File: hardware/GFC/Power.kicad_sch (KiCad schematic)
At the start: 22 parts, among them J1 BAT, U1 MAX17048G+T10

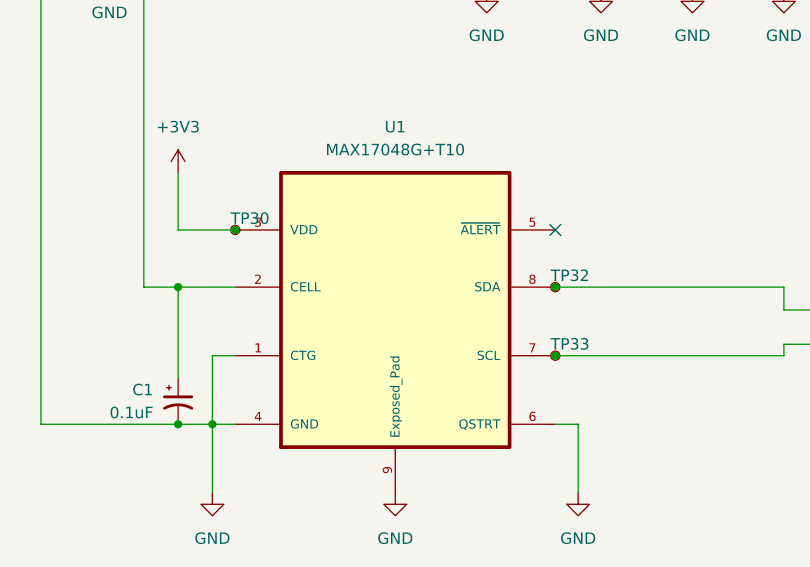
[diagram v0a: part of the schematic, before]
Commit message: Cleaning up the hardware directory
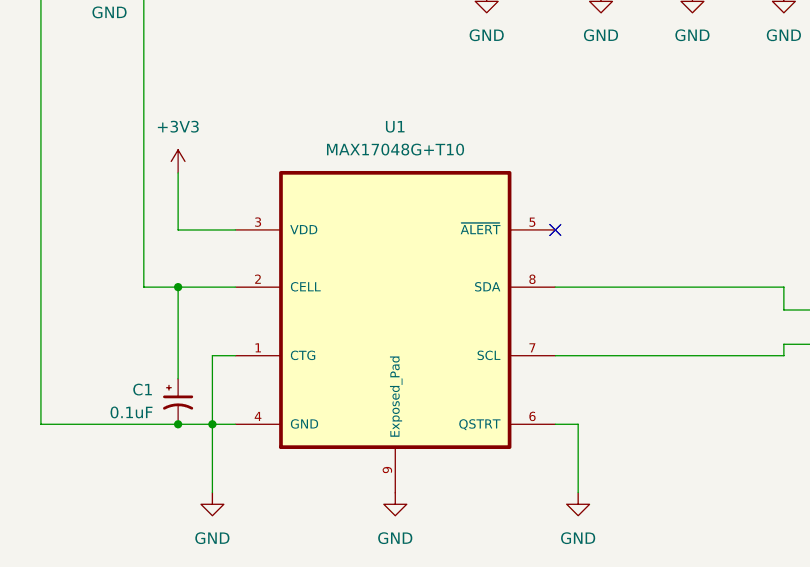
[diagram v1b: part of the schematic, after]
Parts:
- removed TP30, TP32, TP33: Test Point, TestPoint:TestPoint_Pad_D1.0mm, symbol Connector:TestPoint_Small
- R11: footprint Resistor_SMD:R_1206_3216Metric_Pad1.30x1.75mm_HandSolder -> Resistor_SMD:R_0603_1608Metric_Pad0.98x0.95mm_HandSolder
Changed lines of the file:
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@@
   (junction (at 269.24 46.99) (diameter 0) (color 0 0 0 0)
   )
-  (junction (at 107.95 97.79) (diameter 0) (color 0 0 0 0)
-  )
   (junction (at 69.85 113.03) (diameter 0) (color 0 0 0 0)
   )
   (junction (at 252.73 46.99) (diameter 0) (color 0 0 0 0)
-  )
-  (junction (at 107.95 105.41) (diameter 0) (color 0 0 0 0)
-  )
-  (junction (at 72.39 91.44) (diameter 0) (color 0 0 0 0)
   )
   (junction (at 142.24 52.07) (diameter 0) (color 0 0 0 0)
@@
     )
     (property "Datasheet" "" (id 3) (at 266.7 60.96 0)
-      (effects (font (size 1.27 1.27)) hide)
-    )
-    (pin "1")
-  )
-  (symbol (lib_id "Connector:TestPoint_Small") (at 107.95 105.41 0) (mirror y) (unit 1)
-    (in_bom yes) (on_board yes)
-    (property "Reference" "TP33" (id 0) (at 111.76 104.14 0)
-      (effects (font (size 1.27 1.27)) (justify left))
-    )
-    (property "Value" "Test Point" (id 1) (at 106.68 106.6799 0)
-      (effects (font (size 1.27 1.27)) (justify left) hide)
-    )
-    (property "Footprint" "TestPoint:TestPoint_Pad_D1.0mm" (id 2) (at 102.87 105.41 0)
-      (effects (font (size 1.27 1.27)) hide)
-    )
-    (property "Datasheet" "~" (id 3) (at 102.87 105.41 0)
       (effects (font (size 1.27 1.27)) hide)
     )
@@
       (effects (font (size 1.27 1.27)) (justify left))
     )
-    (property "Footprint" "Resistor_SMD:R_1206_3216Metric_Pad1.30x1.75mm_HandSolder" (id 2) (at 238.252 64.77 90)
+    (property "Footprint" "Resistor_SMD:R_0603_1608Metric_Pad0.98x0.95mm_HandSolder" (id 2) (at 238.252 64.77 90)
       (effects (font (size 1.27 1.27)) hide)
     )
@@
     (pin "5")
   )
-  (symbol (lib_id "Connector:TestPoint_Small") (at 72.39 91.44 0) (mirror y) (unit 1)
-    (in_bom yes) (on_board yes)
-    (property "Reference" "TP30" (id 0) (at 76.2 90.17 0)
-      (effects (font (size 1.27 1.27)) (justify left))
-    )
-    (property "Value" "Test Point" (id 1) (at 71.12 92.7099 0)
-      (effects (font (size 1.27 1.27)) (justify left) hide)
-    )
-    (property "Footprint" "TestPoint:TestPoint_Pad_D1.0mm" (id 2) (at 67.31 91.44 0)
-      (effects (font (size 1.27 1.27)) hide)
-    )
-    (property "Datasheet" "~" (id 3) (at 67.31 91.44 0)
-      (effects (font (size 1.27 1.27)) hide)
-    )
-    (pin "1")
-  )
   (symbol (lib_id "Device:C") (at 123.19 60.96 0) (unit 1)
     (in_bom yes) (on_board yes) (fields_autoplaced)
@@
     (pin "2")
   )
-  (symbol (lib_id "Connector:TestPoint_Small") (at 107.95 97.79 0) (mirror y) (unit 1)
-    (in_bom yes) (on_board yes)
-    (property "Reference" "TP32" (id 0) (at 111.76 96.52 0)
-      (effects (font (size 1.27 1.27)) (justify left))
-    )
-    (property "Value" "Test Point" (id 1) (at 106.68 99.0599 0)
-      (effects (font (size 1.27 1.27)) (justify left) hide)
-    )
-    (property "Footprint" "TestPoint:TestPoint_Pad_D1.0mm" (id 2) (at 102.87 97.79 0)
-      (effects (font (size 1.27 1.27)) hide)
-    )
-    (property "Datasheet" "~" (id 3) (at 102.87 97.79 0)
-      (effects (font (size 1.27 1.27)) hide)
-    )
-    (pin "1")
-  )
   (symbol (lib_id "power:PWR_FLAG") (at 39.37 55.88 180) (unit 1)

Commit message: PCB Prototype
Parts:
- removed C18: 0.33uF, Capacitor_SMD:C_0603_1608Metric_Pad1.08x0.95mm_HandSolder, symbol Device:C
- removed C19: 10uF, Capacitor_SMD:C_0805_2012Metric_Pad1.18x1.45mm_HandSolder, symbol Device:C_Polarized
- removed R11: 40k, Resistor_SMD:R_0603_1608Metric_Pad0.98x0.95mm_HandSolder, symbol Device:R
- removed R12: 100k, Resistor_SMD:R_0603_1608Metric_Pad0.98x0.95mm_HandSolder, symbol Device:R
- removed TP29, TP31, TP34, TP35, TP36: Test Point, TestPoint:TestPoint_Pad_D1.0mm, symbol Connector:TestPoint_Small
- removed VR2: LD29150PTR, footprints:LD29150PTR, symbol LDV VReg:LD29150PTR
- J1: footprint TerminalBlock_Phoenix:TerminalBlock_Phoenix_PT-1,5-2-5.0-H_1x02_P5.00mm_Horizontal -> Connector_PinHeader_2.54mm:PinHeader_1x02_P2.54mm_Vertical

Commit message: Update
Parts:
- renumbered C1 to C14, C2 to C15, C3 to C16, C4 to C17, C5 to C18, J1 to J2, U1 to U2
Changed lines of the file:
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@@
   (symbol (lib_id "power:GND") (at 90.17 120.65 0) (unit 1)
     (in_bom yes) (on_board yes) (fields_autoplaced)
-    (property "Reference" "#PWR0143" (id 0) (at 90.17 127 0)
+    (property "Reference" "#PWR0125" (id 0) (at 90.17 127 0)
       (effects (font (size 1.27 1.27)) hide)
     )
@@
   (symbol (lib_id "power:PWR_FLAG") (at 39.37 50.8 0) (mirror y) (unit 1)
     (in_bom yes) (on_board yes) (fields_autoplaced)
-    (property "Reference" "#FLG0101" (id 0) (at 39.37 48.895 0)
+    (property "Reference" "#FLG0105" (id 0) (at 39.37 48.895 0)
       (effects (font (size 1.27 1.27)) hide)
     )
@@
   (symbol (lib_id "MAX17048G_T10:MAX17048G+T10") (at 90.17 100.33 0) (unit 1)
     (in_bom yes) (on_board yes) (fields_autoplaced)
-    (property "Reference" "U1" (id 0) (at 90.17 80.01 0))
+    (property "Reference" "U2" (id 0) (at 90.17 80.01 0))
     (property "Value" "MAX17048G+T10" (id 1) (at 90.17 82.55 0))
     (property "Footprint" "MAX17048G_T10:SON50P200X200X80-9N" (id 2) (at 90.17 100.33 0)
@@
   (symbol (lib_id "Device:C") (at 100.33 60.96 0) (unit 1)
     (in_bom yes) (on_board yes) (fields_autoplaced)
-    (property "Reference" "C2" (id 0) (at 104.14 59.6899 0)
+    (property "Reference" "C15" (id 0) (at 104.14 59.6899 0)
       (effects (font (size 1.27 1.27)) (justify left))
     )
@@
   (symbol (lib_id "power:+3V3") (at 66.04 85.09 0) (unit 1)
     (in_bom yes) (on_board yes) (fields_autoplaced)
-    (property "Reference" "#PWR0140" (id 0) (at 66.04 88.9 0)
+    (property "Reference" "#PWR0134" (id 0) (at 66.04 88.9 0)
       (effects (font (size 1.27 1.27)) hide)
     )
@@
   (symbol (lib_id "power:GND") (at 113.03 64.77 0) (unit 1)
     (in_bom yes) (on_board yes) (fields_autoplaced)
-    (property "Reference" "#PWR0146" (id 0) (at 113.03 71.12 0)
+    (property "Reference" "#PWR0128" (id 0) (at 113.03 71.12 0)
       (effects (font (size 1.27 1.27)) hide)
     )
@@
   (symbol (lib_id "power:GND") (at 58.42 62.23 0) (unit 1)
     (in_bom yes) (on_board yes) (fields_autoplaced)
-    (property "Reference" "#PWR0141" (id 0) (at 58.42 68.58 0)
+    (property "Reference" "#PWR0133" (id 0) (at 58.42 68.58 0)
       (effects (font (size 1.27 1.27)) hide)
     )
@@
   (symbol (lib_id "power:GND") (at 69.85 120.65 0) (unit 1)
     (in_bom yes) (on_board yes) (fields_autoplaced)
-    (property "Reference" "#PWR0144" (id 0) (at 69.85 127 0)
+    (property "Reference" "#PWR0124" (id 0) (at 69.85 127 0)
       (effects (font (size 1.27 1.27)) hide)
     )
@@
   (symbol (lib_id "power:GND") (at 123.19 64.77 0) (unit 1)
     (in_bom yes) (on_board yes) (fields_autoplaced)
-    (property "Reference" "#PWR0137" (id 0) (at 123.19 71.12 0)
+    (property "Reference" "#PWR0127" (id 0) (at 123.19 71.12 0)
       (effects (font (size 1.27 1.27)) hide)
     )
@@
   (symbol (lib_id "power:VCC") (at 66.04 45.72 0) (unit 1)
     (in_bom yes) (on_board yes) (fields_autoplaced)
-    (property "Reference" "#PWR0151" (id 0) (at 66.04 49.53 0)
+    (property "Reference" "#PWR0132" (id 0) (at 66.04 49.53 0)
       (effects (font (size 1.27 1.27)) hide)
     )
@@
   (symbol (lib_id "power:GND") (at 110.49 120.65 0) (unit 1)
     (in_bom yes) (on_board yes) (fields_autoplaced)
-    (property "Reference" "#PWR0145" (id 0) (at 110.49 127 0)
+    (property "Reference" "#PWR0126" (id 0) (at 110.49 127 0)
       (effects (font (size 1.27 1.27)) hide)
     )
@@
   (symbol (lib_id "Device:C_Polarized_Small_US") (at 66.04 110.49 0) (unit 1)
     (in_bom yes) (on_board yes)
-    (property "Reference" "C1" (id 0) (at 60.96 109.22 0)
+    (property "Reference" "C14" (id 0) (at 60.96 109.22 0)
       (effects (font (size 1.27 1.27)) (justify left))
     )
@@
   (symbol (lib_id "Device:C") (at 113.03 60.96 0) (unit 1)
     (in_bom yes) (on_board yes) (fields_autoplaced)
-    (property "Reference" "C3" (id 0) (at 116.84 59.6899 0)
+    (property "Reference" "C16" (id 0) (at 116.84 59.6899 0)
       (effects (font (size 1.27 1.27)) (justify left))
     )
@@
   (symbol (lib_id "Connector:Screw_Terminal_01x02") (at 53.34 52.07 0) (mirror y) (unit 1)
     (in_bom yes) (on_board yes) (fields_autoplaced)
-    (property "Reference" "J1" (id 0) (at 53.34 45.72 0))
+    (property "Reference" "J2" (id 0) (at 53.34 45.72 0))
     (property "Value" "BAT" (id 1) (at 53.34 48.26 0))
     (property "Footprint" "Connector_PinHeader_2.54mm:PinHeader_1x02_P2.54mm_Vertical" (id 2) (at 53.34 52.07 0)
@@
   (symbol (lib_id "power:PWR_FLAG") (at 111.76 52.07 0) (mirror y) (unit 1)
     (in_bom yes) (on_board yes) (fields_autoplaced)
-    (property "Reference" "#FLG0103" (id 0) (at 111.76 50.165 0)
+    (property "Reference" "#FLG0102" (id 0) (at 111.76 50.165 0)
       (effects (font (size 1.27 1.27)) hide)
     )
@@
   (symbol (lib_id "Device:C") (at 123.19 60.96 0) (unit 1)
     (in_bom yes) (on_board yes) (fields_autoplaced)
-    (property "Reference" "C4" (id 0) (at 127 59.6899 0)
+    (property "Reference" "C17" (id 0) (at 127 59.6899 0)
       (effects (font (size 1.27 1.27)) (justify left))
     )
@@
   (symbol (lib_id "Device:C") (at 142.24 60.96 0) (unit 1)
     (in_bom yes) (on_board yes) (fields_autoplaced)
-    (property "Reference" "C5" (id 0) (at 146.05 59.6899 0)
+    (property "Reference" "C18" (id 0) (at 146.05 59.6899 0)
       (effects (font (size 1.27 1.27)) (justify left))
     )
@@
   (symbol (lib_id "power:PWR_FLAG") (at 39.37 55.88 180) (unit 1)
     (in_bom yes) (on_board yes) (fields_autoplaced)
-    (property "Reference" "#FLG0102" (id 0) (at 39.37 57.785 0)
+    (property "Reference" "#FLG0103" (id 0) (at 39.37 57.785 0)
       (effects (font (size 1.27 1.27)) hide)
     )
@@
   (symbol (lib_id "power:VCC") (at 43.18 50.8 270) (unit 1)
     (in_bom yes) (on_board yes)
-    (property "Reference" "#PWR0153" (id 0) (at 39.37 50.8 0)
+    (property "Reference" "#PWR0135" (id 0) (at 39.37 50.8 0)
       (effects (font (size 1.27 1.27)) hide)
     )
@@
   (symbol (lib_id "power:GND") (at 43.18 55.88 90) (unit 1)
     (in_bom yes) (on_board yes)
-    (property "Reference" "#PWR0152" (id 0) (at 49.53 55.88 0)
+    (property "Reference" "#PWR0136" (id 0) (at 49.53 55.88 0)
       (effects (font (size 1.27 1.27)) hide)
     )
@@
   (symbol (lib_id "power:GND") (at 100.33 64.77 0) (unit 1)
     (in_bom yes) (on_board yes) (fields_autoplaced)
-    (property "Reference" "#PWR0142" (id 0) (at 100.33 71.12 0)
-      (effects (font (size 1.27 1.27)) hide)
-    )
+    (property "Reference" "#PWR0123" (id 0) (at 100.33 71.12 0)
+      (effects (font (size 1.27 1.27)) hide)
+    )
